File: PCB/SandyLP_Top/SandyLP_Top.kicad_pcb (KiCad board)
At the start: 2 copper layers, 74.9 x 39.4 mm, 36 parts

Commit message: オプションが無料になったのでJLCのマーキングを削除。その他シルク位置調整。
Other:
- board text removed: "JLCJLCJLCJLC"
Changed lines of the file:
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@@
 		(fp_arc
 			(start -1.308116 0.190917)
-			(mid 0.05 -0.05)
+			(mid 0.050001 -0.05)
 			(end 0.743353 1.142386)
 			(stroke
@@
 		(fp_arc
 			(start 18.425 1.164174)
-			(mid 19.010771 -0.250053)
+			(mid 19.01077 -0.250057)
 			(end 20.425 -0.835826)
 			(stroke
@@
 		(fp_arc
 			(start 18.44991 16.295746)
-			(mid 17.864148 17.709986)
+			(mid 17.864148 17.709982)
 			(end 16.44991 18.295746)
 			(stroke
@@
 		(fp_arc
 			(start 35.4625 -21.13133)
-			(mid 36.876689 -20.545539)
+			(mid 36.876724 -20.545545)
 			(end 37.4625 -19.13133)
 			(stroke
@@
 		(fp_arc
 			(start -1.308116 0.190917)
-			(mid 0.05 -0.05)
+			(mid 0.050001 -0.05)
 			(end 0.743353 1.142386)
 			(stroke
@@
 		(fp_arc
 			(start -1.308116 0.190917)
-			(mid 0.05 -0.05)
+			(mid 0.050001 -0.05)
 			(end 0.743353 1.142386)
 			(stroke
@@
 		(fp_arc
 			(start -1.308116 0.190917)
-			(mid 0.05 -0.05)
+			(mid 0.050001 -0.05)
 			(end 0.743353 1.142386)
 			(stroke
@@
 		(fp_arc
 			(start -1.308116 0.190917)
-			(mid 0.05 -0.05)
+			(mid 0.050001 -0.05)
 			(end 0.743353 1.142386)
 			(stroke
@@
 		(fp_arc
 			(start -1.308116 0.190917)
-			(mid 0.050001 -0.05)
+			(mid 0.05 -0.05)
 			(end 0.743353 1.142386)
 			(stroke
@@
 		)
 	)
-	(gr_text "JLCJLCJLCJLC"
-		(at 193.69906 46.053405 90)
-		(layer "B.SilkS")
-		(effects
-			(font
-				(size 1.5 1.5)
-				(thickness 0.3)
-			)
-			(justify mirror)
-		)
-	)
 	(gr_text "Back Side"
-		(at 187.80531 36.528405 0)
+		(at 157.98031 55.578405 0)
 		(layer "B.SilkS" knockout)
 		(effects
 			(font
-				(size 1.6 1.6)
+				(size 1.8 1.8)
 				(thickness 0.2)
 				(italic yes)
@@
 		)
 	)
-	(gr_text "#SandyLP_kbd DN0010\nTop by @jpskenn"
-		(at 162.30531 37.478405 0)
+	(gr_text "#SandyLP_kbd DN0010 Top by @jpskenn"
+		(at 193.69906 36.528405 0)
 		(layer "B.SilkS")
 		(effects

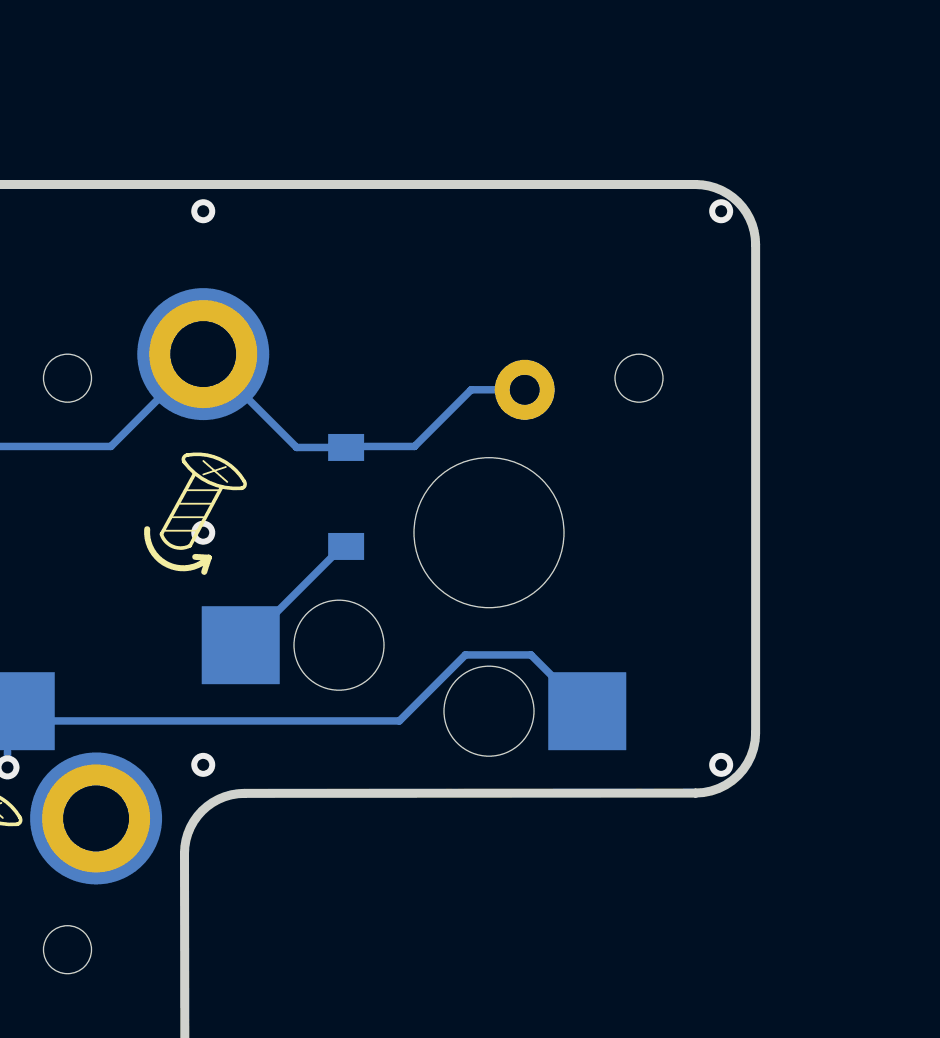
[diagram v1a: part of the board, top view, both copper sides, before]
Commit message: Top基板　ゴムシート貼り付け指標
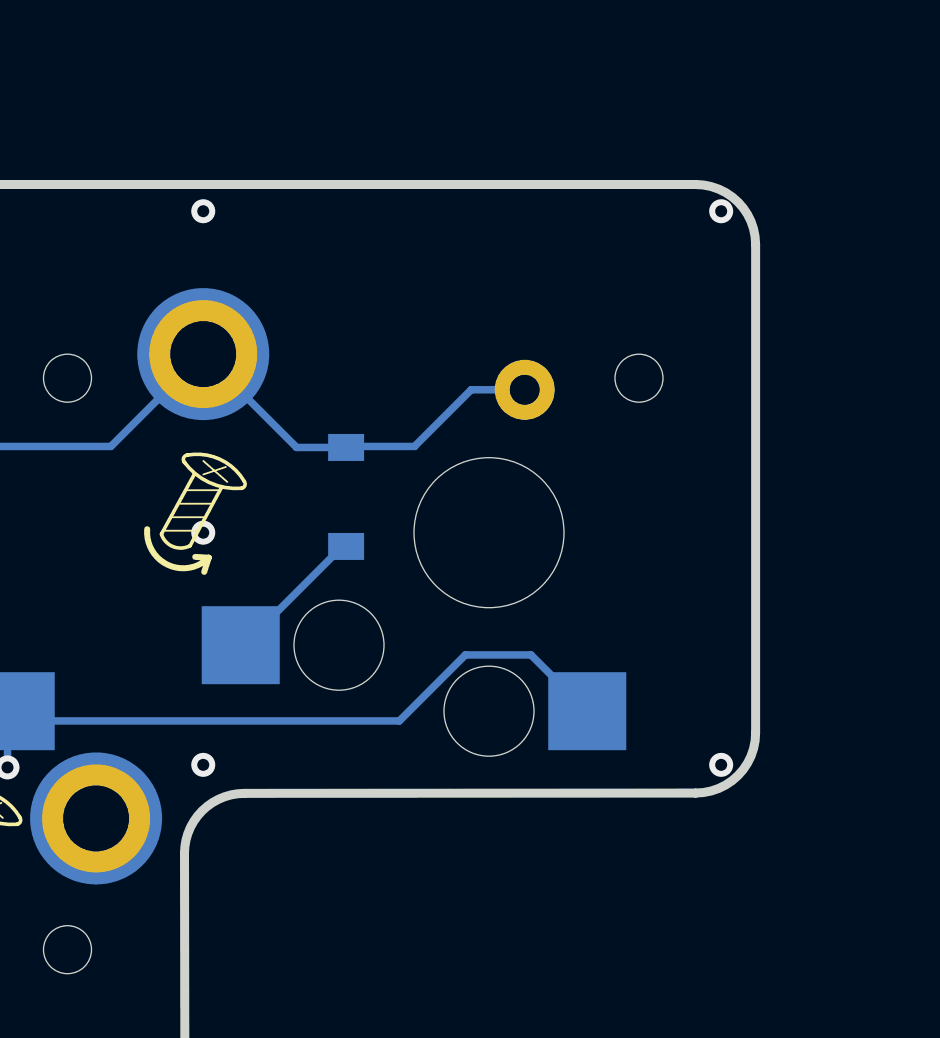
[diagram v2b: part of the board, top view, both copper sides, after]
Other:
- board text added: "#SandyLP_kbd Top"
- board text added: "DN0010"
- board text added: "by @jpskenn"
- board text removed: "#SandyLP_kbd DN0010 Top by @jpskenn"
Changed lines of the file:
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@@
 		(fp_arc
 			(start -1.308116 0.190917)
-			(mid 0.050001 -0.05)
+			(mid 0.05 -0.05)
 			(end 0.743353 1.142386)
 			(stroke
@@
 		(fp_arc
 			(start 18.425 1.164174)
-			(mid 19.01077 -0.250057)
+			(mid 19.010771 -0.250053)
 			(end 20.425 -0.835826)
 			(stroke
@@
 		(fp_arc
 			(start 18.44991 16.295746)
-			(mid 17.864148 17.709982)
+			(mid 17.864148 17.709986)
 			(end 16.44991 18.295746)
 			(stroke
@@
 		(fp_arc
 			(start 35.4625 -21.13133)
-			(mid 36.876724 -20.545545)
+			(mid 36.876689 -20.545539)
 			(end 37.4625 -19.13133)
 			(stroke
@@
 		(fp_arc
 			(start -1.308116 0.190917)
-			(mid 0.050001 -0.05)
+			(mid 0.05 -0.05)
 			(end 0.743353 1.142386)
 			(stroke
@@
 		(fp_arc
 			(start -1.308116 0.190917)
-			(mid 0.050001 -0.05)
+			(mid 0.05 -0.05)
 			(end 0.743353 1.142386)
 			(stroke
@@
 		(fp_arc
 			(start -1.308116 0.190917)
-			(mid 0.050001 -0.05)
+			(mid 0.05 -0.05)
 			(end 0.743353 1.142386)
 			(stroke
@@
 		(fp_arc
 			(start -1.308116 0.190917)
-			(mid 0.050001 -0.05)
+			(mid 0.05 -0.05)
 			(end 0.743353 1.142386)
 			(stroke
@@
 		(fp_arc
 			(start -1.308116 0.190917)
-			(mid 0.05 -0.05)
+			(mid 0.050001 -0.05)
 			(end 0.743353 1.142386)
 			(stroke
@@
 		(tags "test point THT pad")
 		(property "Reference" "EXT_TR0"
-			(at -0.0125 2.034375 0)
+			(at -0.0125 2.64375 0)
 			(layer "B.SilkS")
 			(effects
@@
 		(tags "test point THT pad")
 		(property "Reference" "EXT_TR4"
-			(at 0 1.998 0)
+			(at -4.121875 -1.35625 0)
 			(layer "B.SilkS")
 			(effects
@@
 		(tags "test point THT pad")
 		(property "Reference" "EXT_TC3"
-			(at 0 1.998 0)
+			(at -4.553125 -1.35625 0)
 			(layer "B.SilkS")
 			(effects
@@
 		(tags "test point THT pad")
 		(property "Reference" "EXT_TC4"
-			(at 0 1.998 0)
+			(at 0 4.528125 90)
 			(layer "B.SilkS")
 			(effects
@@
 		(tags "test point THT pad")
 		(property "Reference" "EXT_TR1"
-			(at 0 2.1625 0)
+			(at -4.103125 -1.30625 0)
 			(layer "B.SilkS")
 			(effects
@@
 		)
 	)
+	(gr_line
+		(start 152.36781 59.647155)
+		(end 148.86781 59.647155)
+		(stroke
+			(width 0.5)
+			(type default)
+		)
+		(layer "B.SilkS")
+	)
+	(gr_rect
+		(start 146.61781 35.147155)
+		(end 169.36781 39.647155)
+		(stroke
+			(width 0.5)
+			(type solid)
+		)
+		(fill none)
+		(layer "B.SilkS")
+	)
+	(gr_line
+		(start 145.36781 55.147155)
+		(end 168.06781 55.147155)
+		(stroke
+			(width 0.5)
+			(type default)
+		)
+		(layer "B.SilkS")
+	)
+	(gr_rect
+		(start 181.86781 35.147155)
+		(end 193.86781 39.647155)
+		(stroke
+			(width 0.5)
+			(type solid)
+		)
+		(fill none)
+		(layer "B.SilkS")
+	)
+	(gr_line
+		(start 168.06781 55.147155)
+		(end 168.06781 59.647155)
+		(stroke
+			(width 0.5)
+			(type default)
+		)
+		(layer "B.SilkS")
+	)
+	(gr_line
+		(start 145.61781 59.647155)
+		(end 145.36781 59.647155)
+		(stroke
+			(width 0.5)
+			(type default)
+		)
+		(layer "B.SilkS")
+	)
+	(gr_rect
+		(start 134.36781 43.147155)
+		(end 138.36781 50.647155)
+		(stroke
+			(width 0.5)
+			(type solid)
+		)
+		(fill none)
+		(layer "B.SilkS")
+	)
+	(gr_line
+		(start 171.36781 58.647155)
+		(end 175.61781 58.647155)
+		(stroke
+			(width 0.5)
+			(type default)
+		)
+		(layer "B.SilkS")
+	)
+	(gr_rect
+		(start 172.51781 43.647155)
+		(end 176.51781 51.147155)
+		(stroke
+			(width 0.5)
+			(type solid)
+		)
+		(fill none)
+		(layer "B.SilkS")
+	)
+	(gr_line
+		(start 175.61781 58.647155)
+		(end 175.61781 69.147155)
+		(stroke
+			(width 0.5)
+			(type default)
+		)
+		(layer "B.SilkS")
+	)
+	(gr_line
+		(start 145.36781 59.647155)
+		(end 145.36781 55.147155)
+		(stroke
+			(width 0.5)
+			(type default)
+		)
+		(layer "B.SilkS")
+	)
+	(gr_line
+		(start 171.36781 69.147155)
+		(end 171.36781 58.647155)
+		(stroke
+			(width 0.5)
+			(type default)
+		)
+		(layer "B.SilkS")
+	)
+	(gr_rect
+		(start 121.96781 35.147155)
+		(end 133.96781 39.647155)
+		(stroke
+			(width 0.5)
+			(type solid)
+		)
+		(fill none)
+		(layer "B.SilkS")
+	)
+	(gr_line
+		(start 175.61781 69.147155)
+		(end 175.11781 69.147155)
+		(stroke
+			(width 0.5)
+			(type default)
+		)
+		(layer "B.SilkS")
+	)
+	(gr_line
+		(start 168.06781 59.647155)
+		(end 154.56781 59.647155)
+		(stroke
+			(width 0.5)
+			(type default)
+		)
+		(layer "B.SilkS")
+	)
+	(gr_line
+		(start 171.86781 69.147155)
+		(end 171.36781 69.147155)
+		(stroke
+			(width 0.5)
+			(type default)
+		)
+		(layer "B.SilkS")
+	)
+	(gr_text "DN0010"
+		(at 193.36781 37.147155 0)
+		(layer "B.SilkS")
+		(effects
+			(font
+				(size 1.5 1.5)
+				(thickness 0.15)
+			)
+			(justify left mirror)
+		)
+	)
+	(gr_text "by @jpskenn"
+		(at 137.36781 36.647155 0)
+		(layer "B.SilkS")
+		(effects
+			(font
+				(size 1.5 1.5)
+				(thickness 0.15)
+			)
+			(justify left mirror)
+		)
+	)
 	(gr_text "Back Side"
-		(at 157.98031 55.578405 0)
+		(at 157.98031 57.647155 0)
 		(layer "B.SilkS" knockout)
 		(effects
@@
 		)
 	)
-	(gr_text "#SandyLP_kbd DN0010 Top by @jpskenn"
-		(at 193.69906 36.528405 0)
+	(gr_text "#SandyLP_kbd Top"
+		(at 168.86781 37.147155 0)
 		(layer "B.SilkS")
 		(effects
